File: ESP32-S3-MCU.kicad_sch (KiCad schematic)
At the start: 39 parts, among them SW1 RESET, SW2 BOOT, X1 32.768KHz

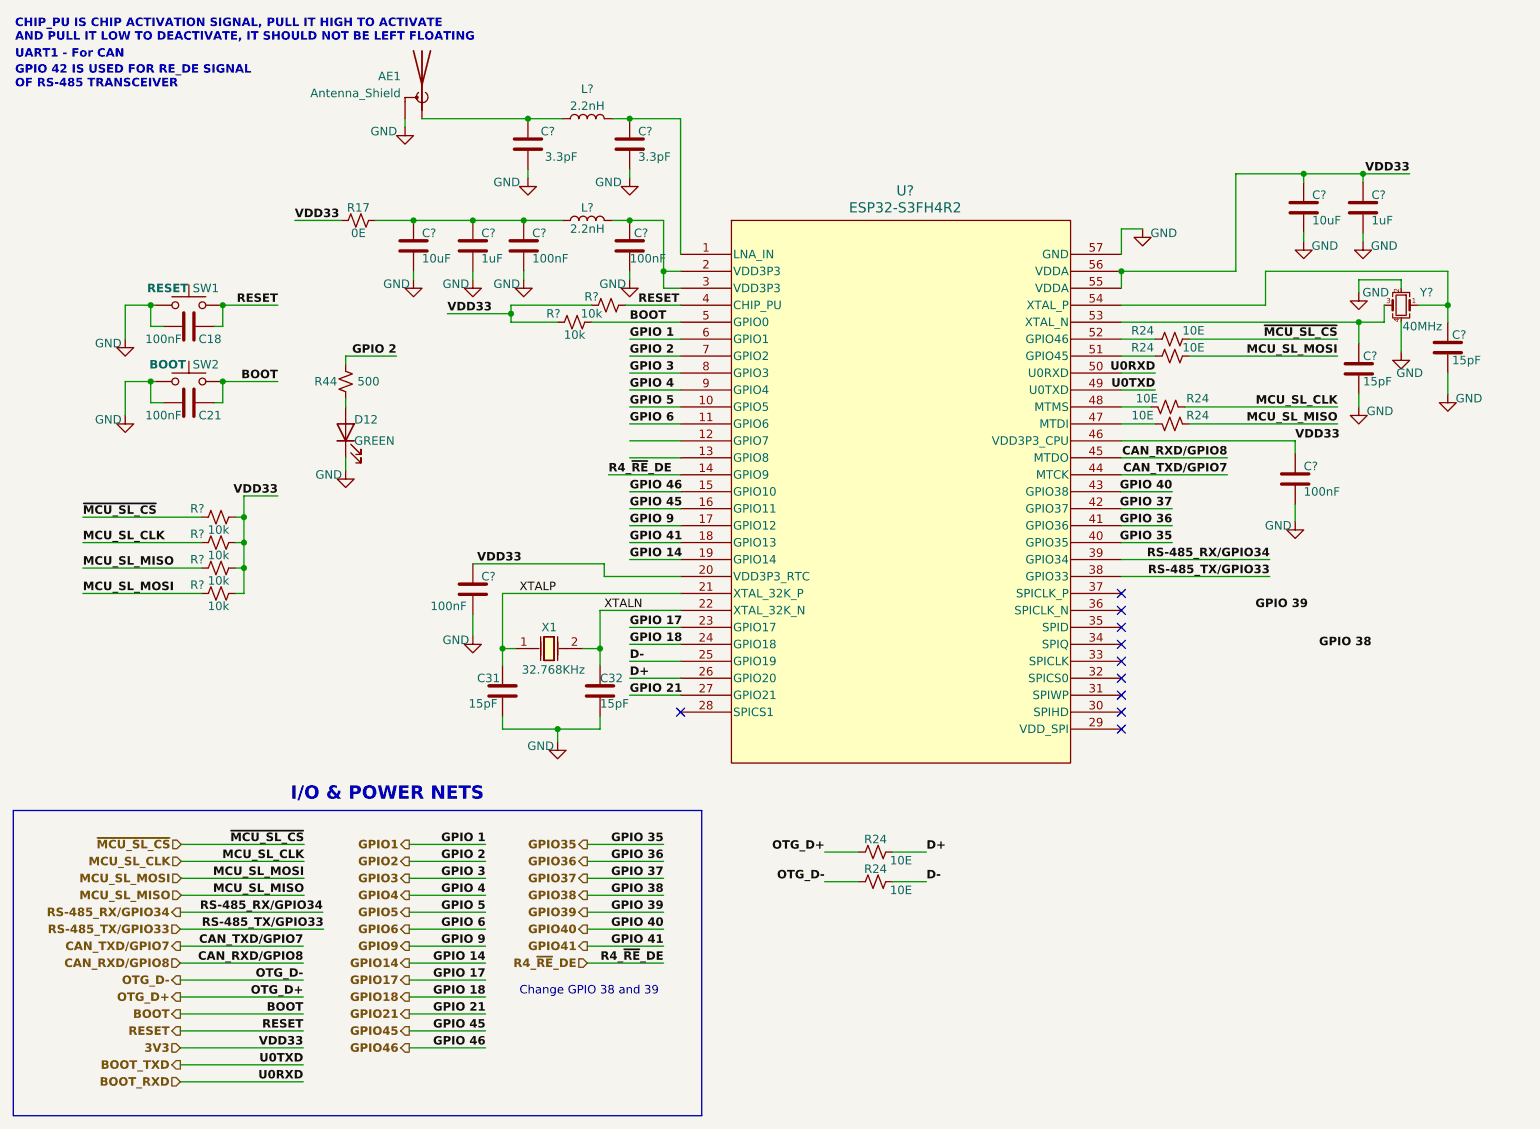
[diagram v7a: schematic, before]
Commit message: Added selection jumper block diagram and solved DRC errors
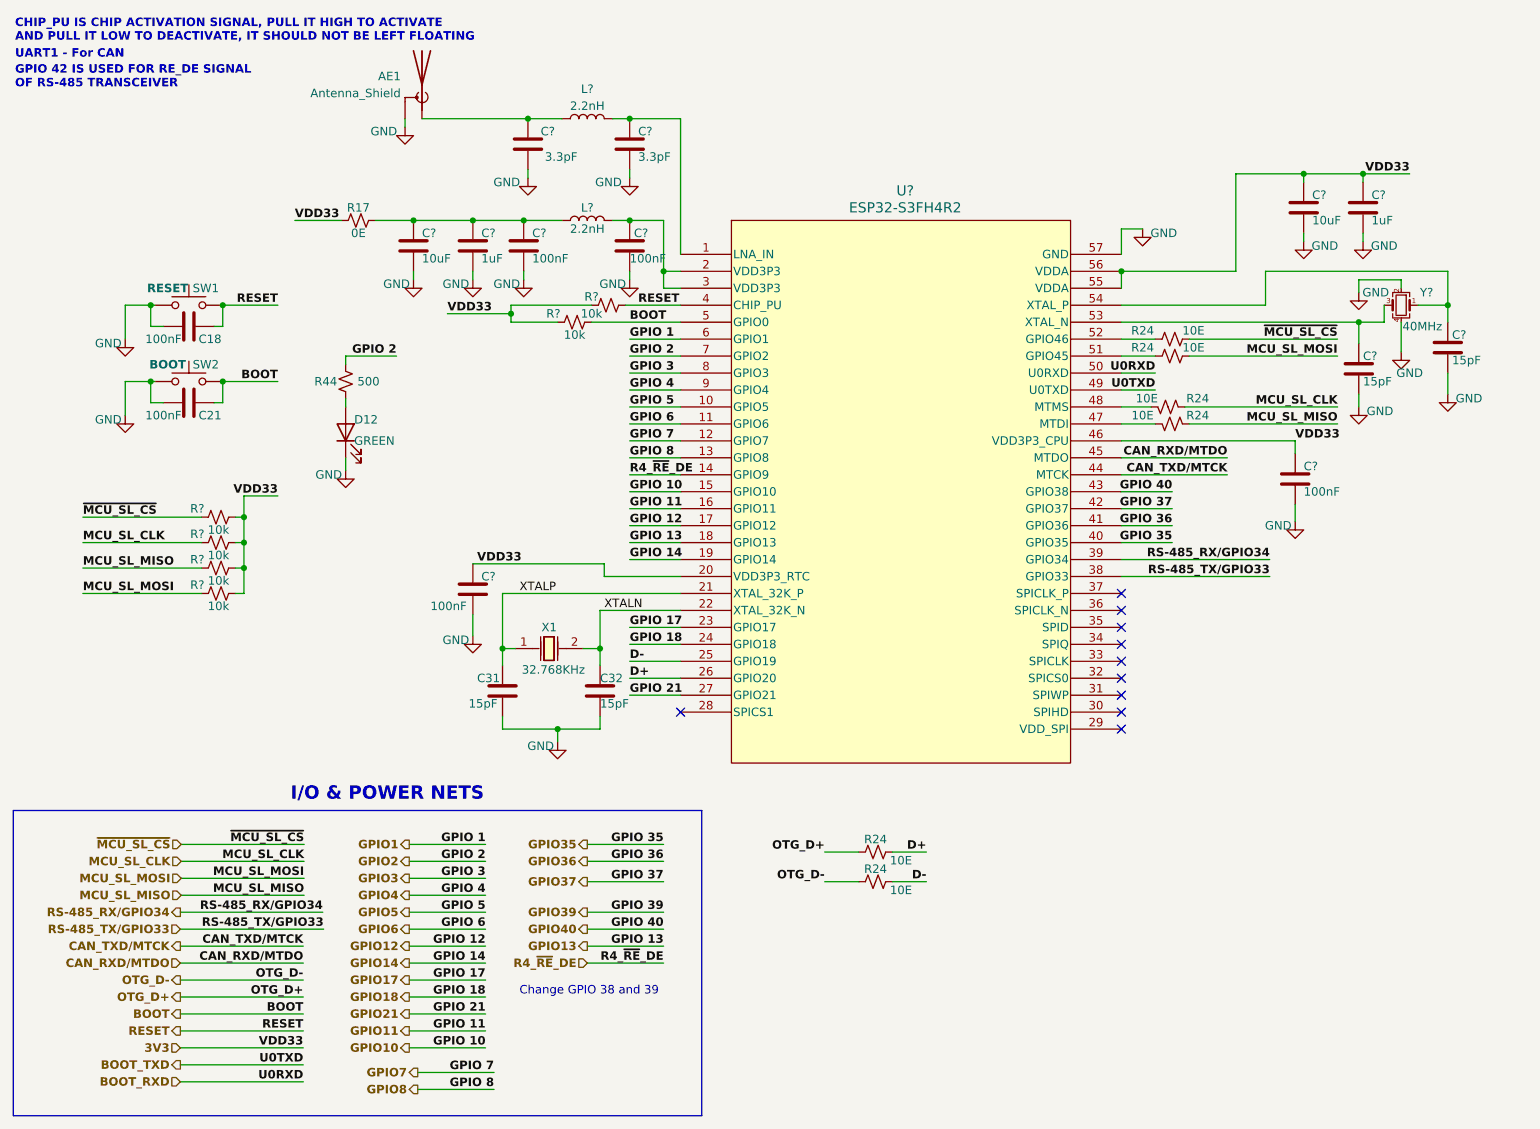
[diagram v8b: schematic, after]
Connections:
- net GPIO7: now reaches U?.12 (GPIO7)
- net GPIO8: now reaches U?.13 (GPIO8)
- net CAN_RXD/GPIO8 renamed CAN_RXD/MTDO
- net CAN_TXD/GPIO7 renamed CAN_TXD/MTCK
- net GPIO41 renamed GPIO13
- net GPIO45 renamed GPIO11
- net GPIO46 renamed GPIO10
- net GPIO9 renamed GPIO12
